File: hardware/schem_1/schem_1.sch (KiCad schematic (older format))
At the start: 41 parts

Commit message: add 128x32 oled to schem. add new symbols to library. add backup power (supercap) circuit. update plan. add esp32 pinouts
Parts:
- removed C? (x5): 10uF, symbol Device:C_Small
- removed C?: 100uF, symbol Device:CP
- removed C? (x2): 0.1uF, symbol Device:C_Small
- removed C?: 5F, symbol Device:CP
- removed D?: D_Schottky, symbol Device:D_Schottky
- removed J?: USB_B_Mini, symbol Connector:USB_B_Mini
- removed Q?: Q_PMOS_DGS, symbol Device:Q_PMOS_DGS
- removed R?: 1k, symbol Device:R
- removed R?: 10k, symbol Device:R
- removed R?: 82k, symbol Device:R
- removed R?: 100k, symbol Device:R
- removed U?: ESP32-S2-WROVER, RF_Module:ESP32-S2-WROVER, symbol RF_Module:ESP32-S2-WROVER
- removed U?: AMS1117, Package_TO_SOT_SMD:SOT-223-3_TabPin2, symbol Regulator_Linear:AMS1117
- removed U?: XC6206-1.2V, Package_TO_SOT_SMD:SOT-23, symbol Regulator_Linear:XC6206PxxxMR
- removed U?: XC6206-2.8V, Package_TO_SOT_SMD:SOT-23, symbol Regulator_Linear:XC6206PxxxMR
- added C?: 0.1uF, symbol Device:C_Small
- added C? (x2): 1uF, symbol Device:C_Small
- added R?: 0R, symbol Device:R_Small
- added R?: 10K, symbol Device:R_Small
- added R? (x3): 10k, symbol Device:R_Small
- added SW?: BTN_BOOT, symbol Switch:SW_Push
- added U?: ESP32-WROOM-32D, RF_Module:ESP32-WROOM-32, symbol RF_Module:ESP32-WROOM-32D
- added U?: ESP-PSRAM32, Package_SO:SOIC-8_3.9x4.9mm_P1.27mm, symbol Memory_RAM:ESP-PSRAM32
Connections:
- net labels added: CLK, CMD, LED_RED, OLED_SCL, OLED_SDA, PSRAM_CLK, PSRAM_CS, SD0, SD1, SD2, SD3, U0RXD, U0TXD
- net labels removed: +5V, PWR_Detect, RED_LED, Vin
- wire segments 142 -> 139
- no-connect marks 2 -> 1
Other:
- note removed: "5.1V down to 2.8V"
- note removed: "5V in from USB, drop to 3V3 for ESP32. Then to 2.8V and 1.2V for camera. \nWhen USB is disconnected, supercapacitor provides power for device to safely shut down."
- note removed: "ESP32 WROVER has PSRAM built in"
- note removed: "Power"
- moved on the sheet: C?, D?, J?, R?

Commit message: update schematic: add io expander with peripherals, update power circuitry- change some components. update project plan. update footprints
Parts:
- removed D?: RED_LED, symbol Device:LED
- removed Q?: 2N3904, Package_TO_SOT_THT:TO-92_Inline, symbol Transistor_BJT:2N3904
- removed R?: 261R, symbol Device:R
- removed R?: 10k, symbol Device:R
- added J4: Conn_01x03_Female, Connector_PinSocket_2.54mm:PinSocket_1x03_P2.54mm_Vertical, symbol Connector:Conn_01x03_Female
- C1, C2, C3, C4, C5, C6, C7: renamed from C?; footprint (none) -> Capacitor_SMD:C_0603_1608Metric
- J1: renamed from J?; footprint (none) -> Connector_FFC-FPC:TE_2-1734839-4_1x24-1MP_P0.5mm_Horizontal
- J2: renamed from J?; footprint (none) -> Connector_Card:microSD_HC_Hirose_DM3D-SF
- SW1, SW2: renamed from SW?; footprint (none) -> Digikey:Switch_Tactile_SMD_4.5x4.5mm_TL3315NF160Q
- U2: renamed from U?; value ESP-PSRAM32 -> ESP-PSRAM64H
- gave numbers to parts that had none: 16
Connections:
- net labels added: SCL, SDA
- net labels removed: CLK, CMD, LED_RED, OLED_SCL, OLED_SDA
- wire segments 139 -> 137
- no-connect marks 1 -> 3
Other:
- note added: "MicroSD Card"
- note added: "OV7670 Camera"
- note added: "PSRAM"
- note removed: "Forward voltage red LED \nis roughly 2V. \nWant 5 mA across."
- moved on the sheet: C3, C4, C5, C6, C7, J1, J2, R1, R10, R11, R12, R13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

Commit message: Replace ESP32 Wroom module with WRover and remove the external PSRAM (as Wrover has one built in). Create symbol and footprint for Wrover. Update footprints for resistors and buttons. Update USB footprint as it was not matching symbol.
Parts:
- removed C2, C7: 1uF, Capacitor_SMD:C_0603_1608Metric, symbol Device:C_Small
- removed R10: 10K, symbol Device:R_Small
- removed R5, R9: 10k, symbol Device:R_Small
- removed U1: ESP32-WROOM-32D, RF_Module:ESP32-WROOM-32, symbol RF_Module:ESP32-WROOM-32D
- removed U2: ESP-PSRAM64H, Package_SO:SOIC-8_3.9x4.9mm_P1.27mm, symbol Memory_RAM:ESP-PSRAM32
- added C25: 1uF, Capacitor_SMD:C_0603_1608Metric, symbol Device:C_Small
- added C26: 0.1uF, Capacitor_SMD:C_0603_1608Metric, symbol Device:C_Small
- added R26, R27: 10k, Resistor_SMD:R_0603_1608Metric, symbol Device:R_Small
- added U1: ESP32-S2-WROVER-JC, RF_Module:ESP32-WROOM-32, symbol jclib:ESP32-S2-WROVER-JC
- C1: value 0.1uF -> 47uF/6.3V/20%/0805; footprint Capacitor_SMD:C_0603_1608Metric -> Capacitor_SMD:C_0805_2012Metric
- C6: value 0.1uF -> 1uF
- R1, R11, R12, R13, R14, R15, R2, R3, R4, R6, R7, R8: footprint (none) -> Resistor_SMD:R_0603_1608Metric
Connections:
- net labels removed: PSRAM_CLK, PSRAM_CS, SD0, SD1, SD2, SD3
- wire segments 137 -> 127
- no-connect marks 3 -> 11
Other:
- note removed: "PSRAM"
- moved on the sheet: C3, C4, C5, C6, J1, J4, R1, R2, R3, R4, R6, R7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

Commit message: change supercap for one with lower esr and shorter. create footprint and 3d model for new cap. remove power switch entirely.
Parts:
- J4: footprint Connector_PinSocket_2.54mm:PinSocket_1x03_P2.54mm_Vertical -> Connector_PinSocket_2.54mm:PinSocket_1x03_P2.54mm_Horizontal
- U1: footprint RF_Module:ESP32-WROOM-32 -> kicad_lib:ESP32-S2-WROVER_JC
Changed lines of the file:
@@
 F 0 "J4" H 5492 6775 50  0000 C CNN
 F 1 "Conn_01x03_Female" H 5492 6866 50  0000 C CNN
-F 2 "Connector_PinSocket_2.54mm:PinSocket_1x03_P2.54mm_Vertical" H 5600 7100 50  0001 C CNN
+F 2 "Connector_PinSocket_2.54mm:PinSocket_1x03_P2.54mm_Horizontal" H 5600 7100 50  0001 C CNN
 F 3 "~" H 5600 7100 50  0001 C CNN
 	1    5600 7100
@@
 F 0 "U1" H 3950 3917 50  0000 C CNN
 F 1 "ESP32-S2-WROVER-JC" H 3950 3826 50  0000 C CNN
-F 2 "RF_Module:ESP32-WROOM-32" V 4000 2750 50  0001 C CNN
+F 2 "kicad_lib:ESP32-S2-WROVER_JC" V 4000 2750 50  0001 C CNN
 F 3 "" H 3650 2600 50  0001 C CNN
 	1    3950 2550

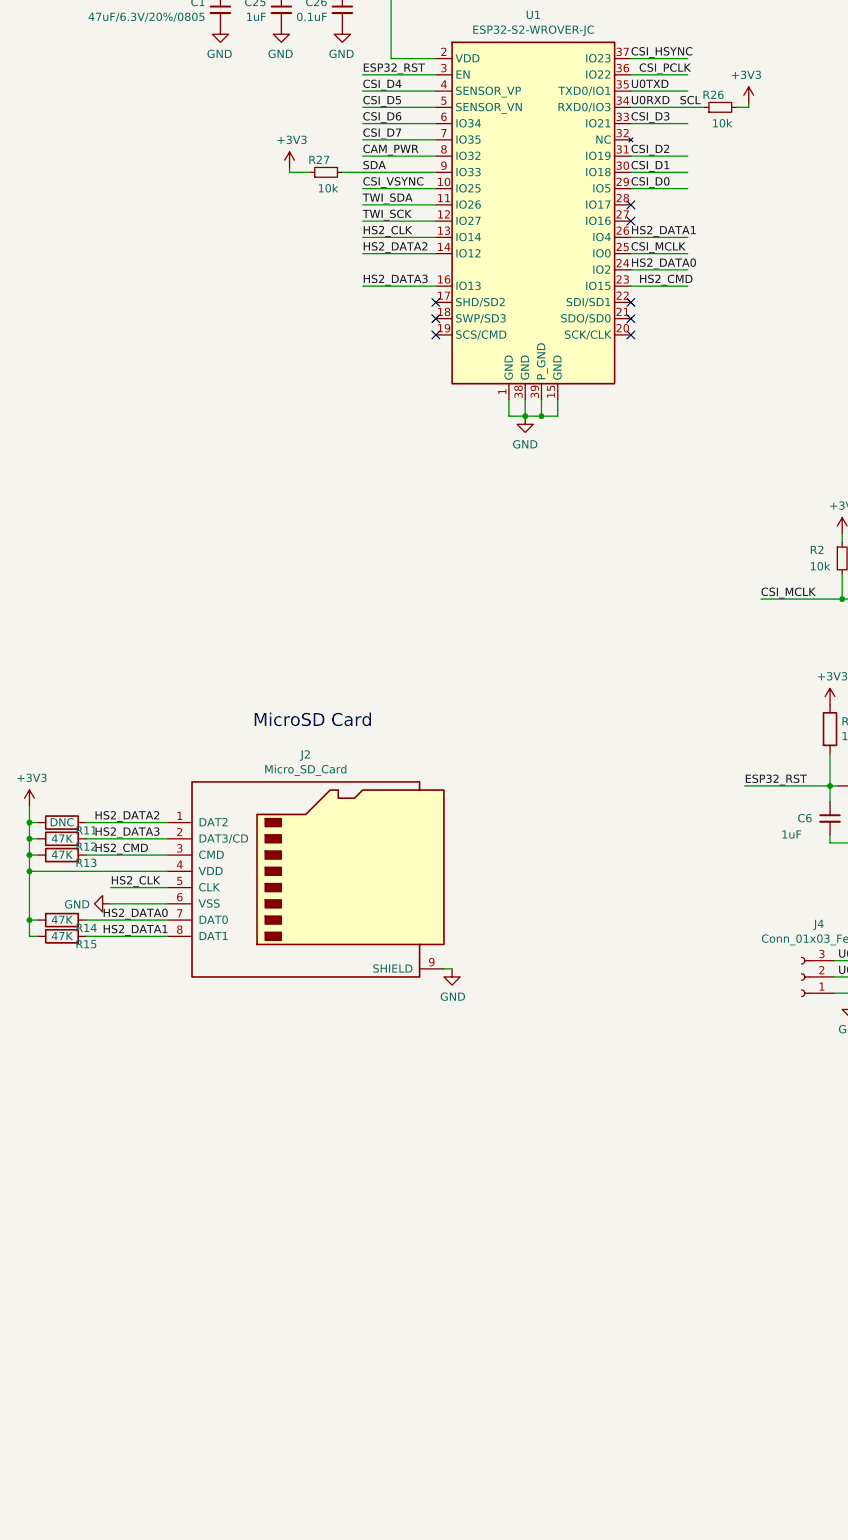
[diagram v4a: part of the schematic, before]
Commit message: update footprints for 24way connector, 3D models. add new connector to connect the two PCB's
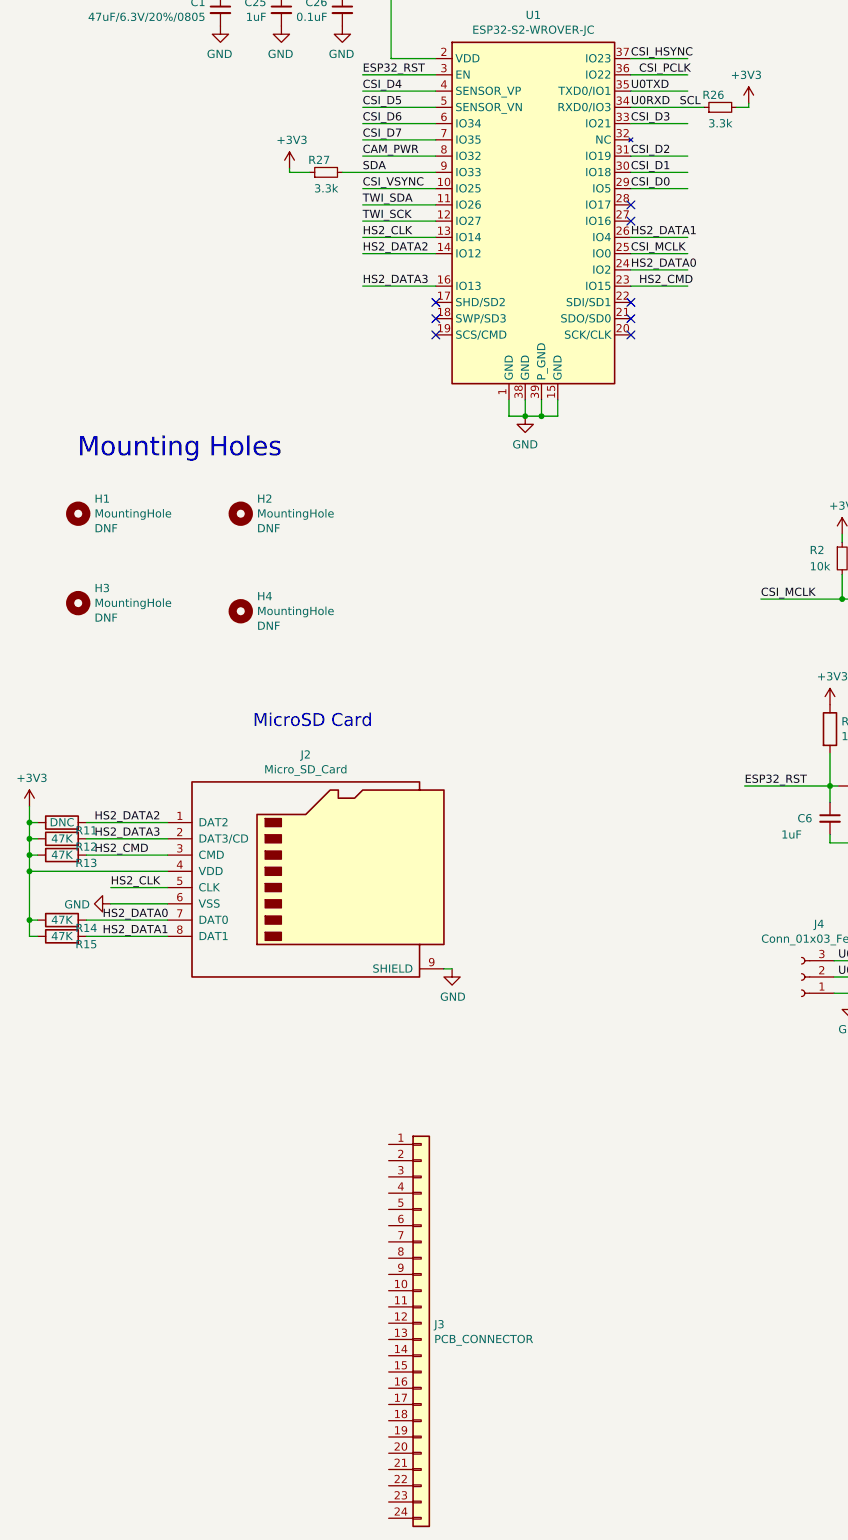
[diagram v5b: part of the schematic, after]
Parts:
- added H1, H2, H3, H4: MountingHole, MountingHole:MountingHole_2mm, symbol Mechanical:MountingHole
- added J3: PCB_CONNECTOR, Connector_FFC-FPC:TE_2-1734839-4_1x24-1MP_P0.5mm_Horizontal, symbol Connector_Generic:Conn_01x24
- R11: DNC (none) -> DNC
- R26, R27: value 10k -> 3.3k
- SW1, SW2: footprint Digikey:Switch_Tactile_SMD_4.5x4.5mm_TL3315NF160Q -> kicad_lib:JC_Switch_TL6330
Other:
- note added: "Mounting Holes"
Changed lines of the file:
@@
 EELAYER 30 0
 EELAYER END
-$Descr A4 11693 8268
+$Descr A3 16535 11693
 encoding utf-8
 Sheet 1 4
@@
 F 0 "SW2" H 5979 6073 50  0000 L CNN
 F 1 "ESP32_RESET" H 6150 6000 50  0000 L CNN
-F 2 "Digikey:Switch_Tactile_SMD_4.5x4.5mm_TL3315NF160Q" H 6025 6125 50  0001 C CNN
+F 2 "kicad_lib:JC_Switch_TL6330" H 6025 6125 50  0001 C CNN
 F 3 "~" H 6025 6125 50  0001 C CNN
 	1    6025 5925
@@
 F 2 "Resistor_SMD:R_0603_1608Metric" V 980 6150 50  0001 C CNN
 F 3 "~" H 1050 6150 50  0001 C CNN
+F 4 "DNC" V 1050 6150 50  0001 C CNN "DNC"
 	1    1050 6150
 	0    -1   -1   0
@@
 F 0 "SW1" H 6175 5060 50  0000 C CNN
 F 1 "BTN_BOOT" H 6175 4969 50  0000 C CNN
-F 2 "Digikey:Switch_Tactile_SMD_4.5x4.5mm_TL3315NF160Q" H 6175 4975 50  0001 C CNN
+F 2 "kicad_lib:JC_Switch_TL6330" H 6175 4975 50  0001 C CNN
 F 3 "~" H 6175 4975 50  0001 C CNN
 	1    6175 4775
@@
 P 5100 1750
 F 0 "R26" V 5175 1725 50  0000 L CNN
-F 1 "10k" V 5000 1675 50  0000 L CNN
+F 1 "3.3k" V 5000 1675 50  0000 L CNN
 F 2 "Resistor_SMD:R_0603_1608Metric" H 5100 1750 50  0001 C CNN
 F 3 "~" H 5100 1750 50  0001 C CNN
@@
 P 2675 2150
 F 0 "R27" V 2750 2125 50  0000 L CNN
-F 1 "10k" V 2575 2075 50  0000 L CNN
+F 1 "3.3k" V 2575 2075 50  0000 L CNN
 F 2 "Resistor_SMD:R_0603_1608Metric" H 2675 2150 50  0001 C CNN
 F 3 "~" H 2675 2150 50  0001 C CNN
@@
 Wire Wire Line
 	4000 3650 4100 3650
+$Comp
+L Mechanical:MountingHole H1
+U 1 1 60CB09A1
+P 1150 4250
+F 0 "H1" H 1250 4341 50  0000 L CNN
+F 1 "MountingHole" H 1250 4250 50  0000 L CNN
+F 2 "MountingHole:MountingHole_2mm" H 1150 4250 50  0001 C CNN
+F 3 "~" H 1150 4250 50  0001 C CNN
+F 4 "DNF" H 1250 4159 50  0000 L CNN "DNF"
+	1    1150 4250
+	1    0    0    -1
+$EndComp
+Text Notes 1145 3915 0    118  ~ 0
+Mounting Holes
+$Comp
+L Mechanical:MountingHole H2
+U 1 1 60CB174E
+P 2150 4250
+F 0 "H2" H 2250 4341 50  0000 L CNN
+F 1 "MountingHole" H 2250 4250 50  0000 L CNN
+F 2 "MountingHole:MountingHole_2mm" H 2150 4250 50  0001 C CNN
+F 3 "~" H 2150 4250 50  0001 C CNN
+F 4 "DNF" H 2250 4159 50  0000 L CNN "DNF"
+	1    2150 4250
+	1    0    0    -1
+$EndComp
+$Comp
+L Mechanical:MountingHole H3
+U 1 1 60CB2EED
+P 1150 4800
+F 0 "H3" H 1250 4891 50  0000 L CNN
+F 1 "MountingHole" H 1250 4800 50  0000 L CNN
+F 2 "MountingHole:MountingHole_2mm" H 1150 4800 50  0001 C CNN
+F 3 "~" H 1150 4800 50  0001 C CNN
+F 4 "DNF" H 1250 4709 50  0000 L CNN "DNF"
+	1    1150 4800
+	1    0    0    -1
+$EndComp
+$Comp
+L Mechanical:MountingHole H4
+U 1 1 60CB391E
+P 2150 4850
+F 0 "H4" H 2250 4941 50  0000 L CNN
+F 1 "MountingHole" H 2250 4850 50  0000 L CNN
+F 2 "MountingHole:MountingHole_2mm" H 2150 4850 50  0001 C CNN
+F 3 "~" H 2150 4850 50  0001 C CNN
+F 4 "DNF" H 2250 4759 50  0000 L CNN "DNF"
+	1    2150 4850
+	1    0    0    -1
+$EndComp
+$Comp
+L Connector_Generic:Conn_01x24 J3
+U 1 1 60D37B99
+P 3260 9230
+F 0 "J3" H 3340 9222 50  0000 L CNN
+F 1 "PCB_CONNECTOR" H 3340 9131 50  0000 L CNN
+F 2 "Connector_FFC-FPC:TE_2-1734839-4_1x24-1MP_P0.5mm_Horizontal" H 3260 9230 50  0001 C CNN
+F 3 "~" H 3260 9230 50  0001 C CNN
+	1    3260 9230
+	1    0    0    -1
+$EndComp
 $EndSCHEMATC

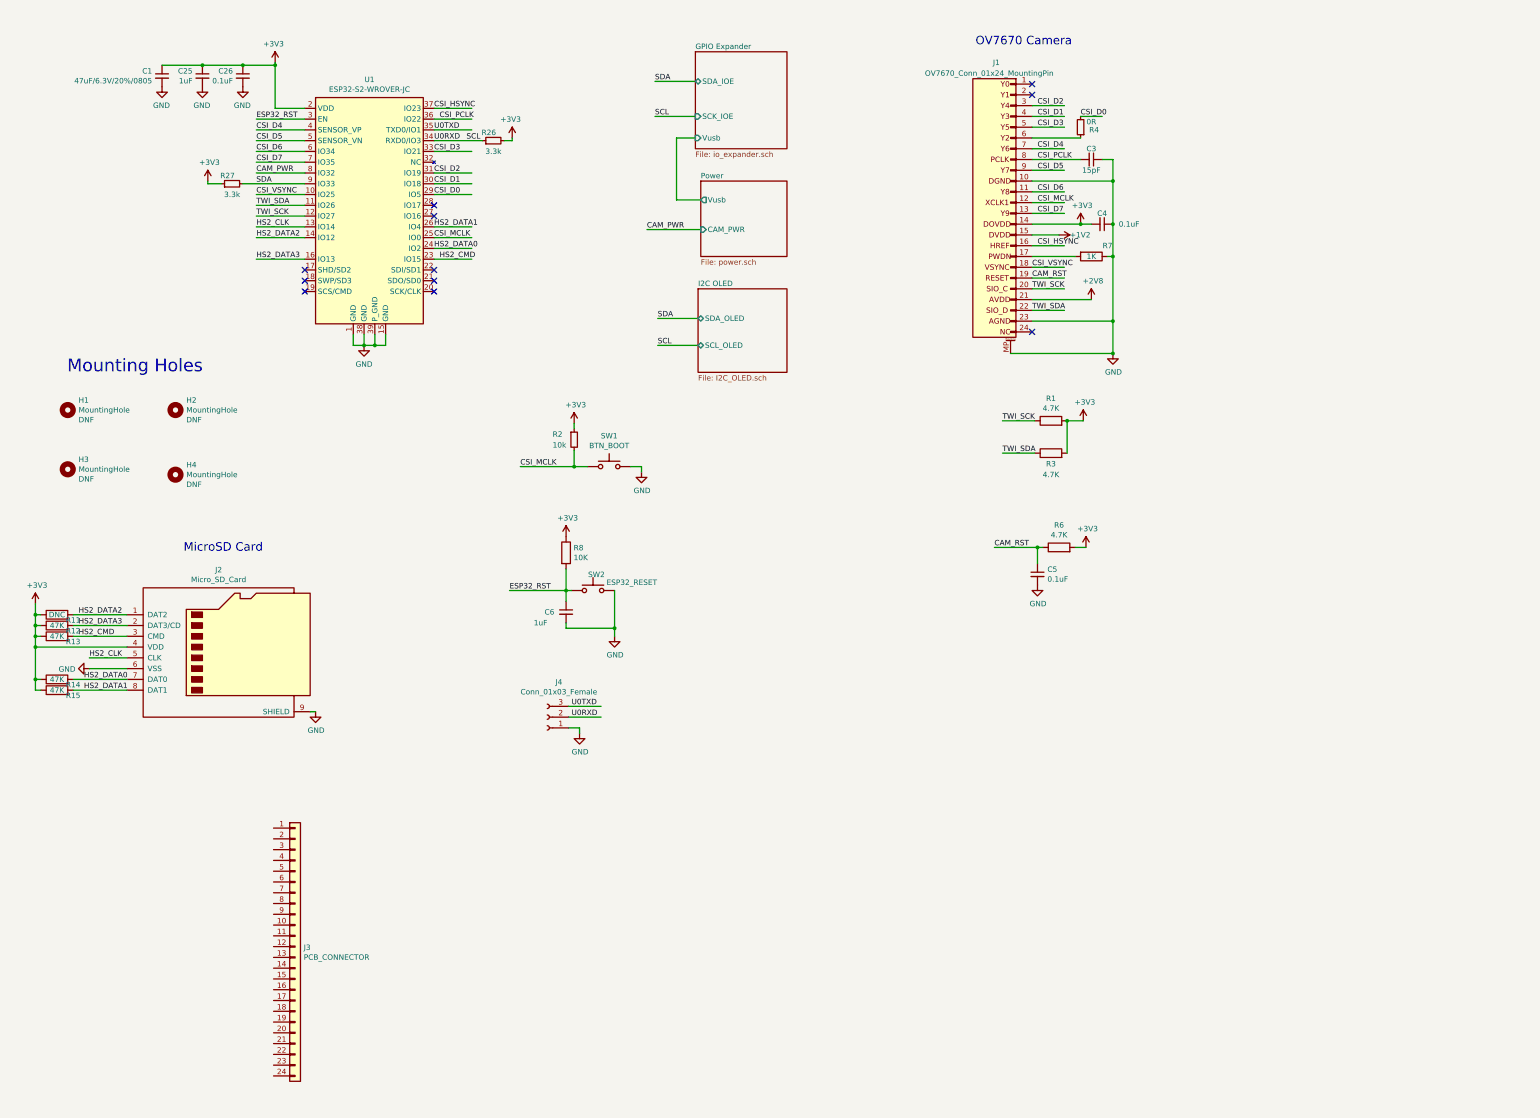
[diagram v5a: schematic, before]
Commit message: add correct 3d model for esp32 wrover e. initial placement of components done for both boards. need to start routing
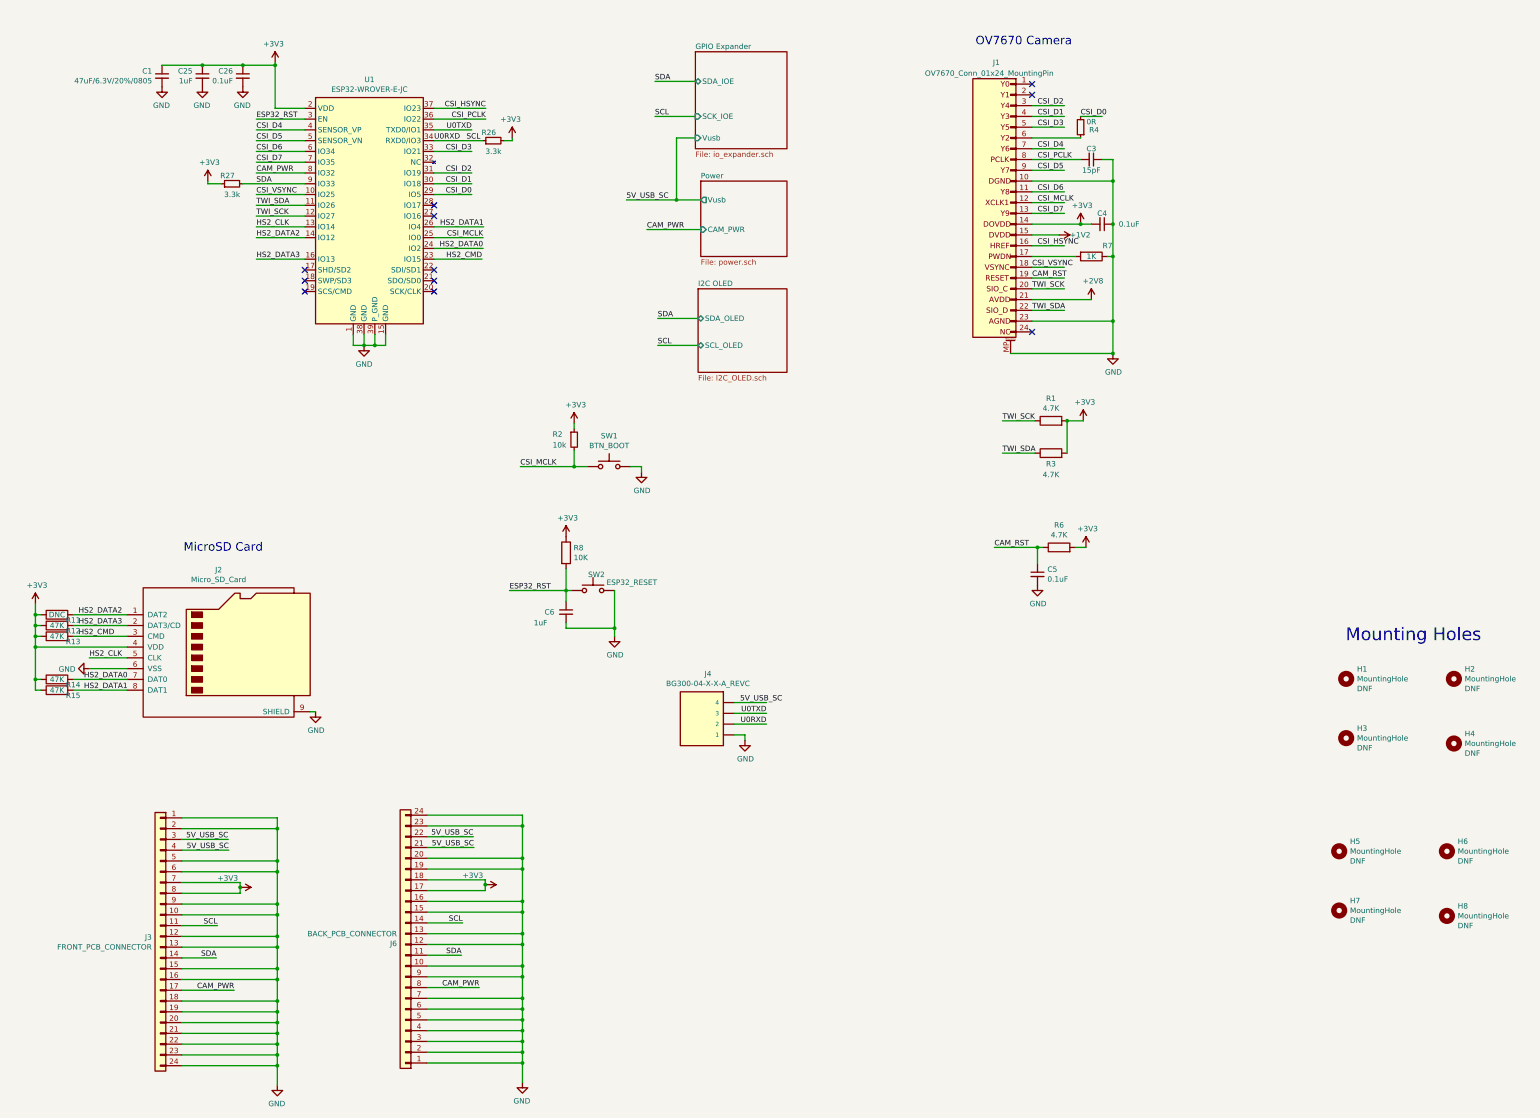
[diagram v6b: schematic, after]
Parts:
- removed J4: Conn_01x03_Female, Connector_PinSocket_2.54mm:PinSocket_1x03_P2.54mm_Horizontal, symbol Connector:Conn_01x03_Female
- removed U1: ESP32-S2-WROVER-JC, kicad_lib:ESP32-S2-WROVER_JC, symbol jclib:ESP32-S2-WROVER-JC
- added H5, H6, H7, H8: MountingHole, MountingHole:MountingHole_2mm, symbol Mechanical:MountingHole
- added J4: BG300-04-X-X-A_REVC, BG300-04-X-X-A_REVC:GCT_BG300-04-X-X-A_REVC, symbol BG300-04-X-X-A_REVC:BG300-04-X-X-A_REVC
- added J6: BACK_PCB_CONNECTOR, Connector_FFC-FPC:TE_2-1734839-4_1x24-1MP_P0.5mm_Horizontal, symbol Connector_Generic:Conn_01x24
- added U1: ESP32-WROVER-E-JC, kicad_lib:ESP32-WROVER-E-JC, symbol jclib:ESP32-WROVER-E-JC
- J3: value PCB_CONNECTOR -> FRONT_PCB_CONNECTOR
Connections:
- net labels added: 5V_USB_SC
- wire segments 127 -> 215
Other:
- moved on the sheet: H1, H2, H3, H4, J3
